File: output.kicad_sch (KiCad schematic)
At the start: 5 parts

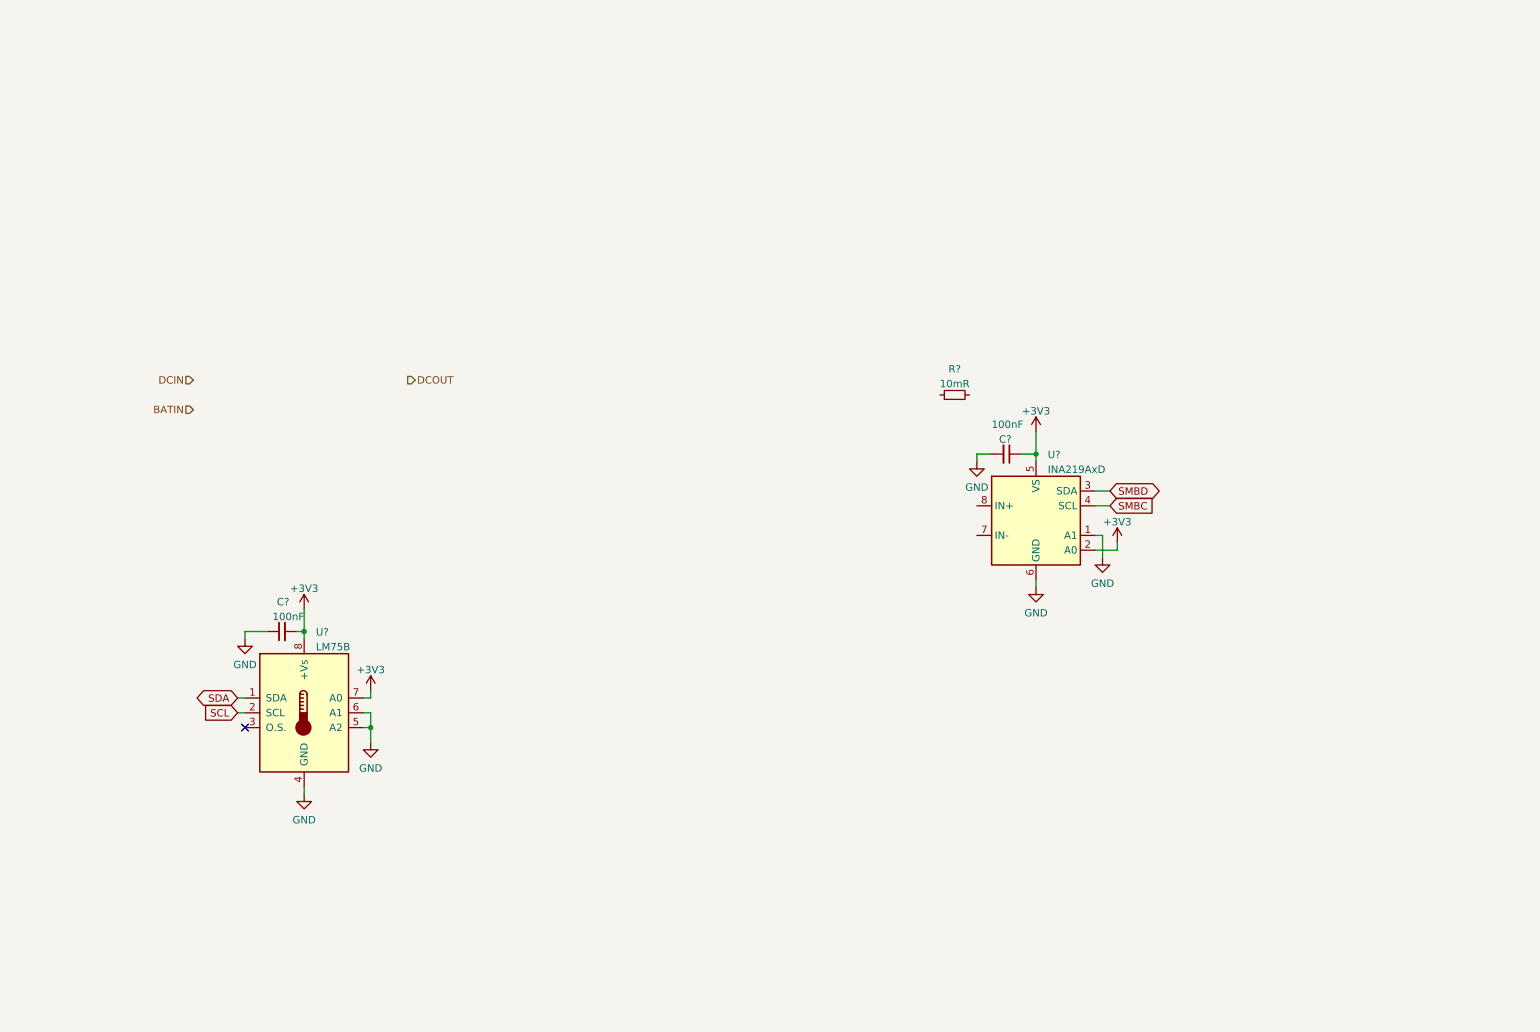
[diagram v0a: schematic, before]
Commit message: Add partial DC output circuitry
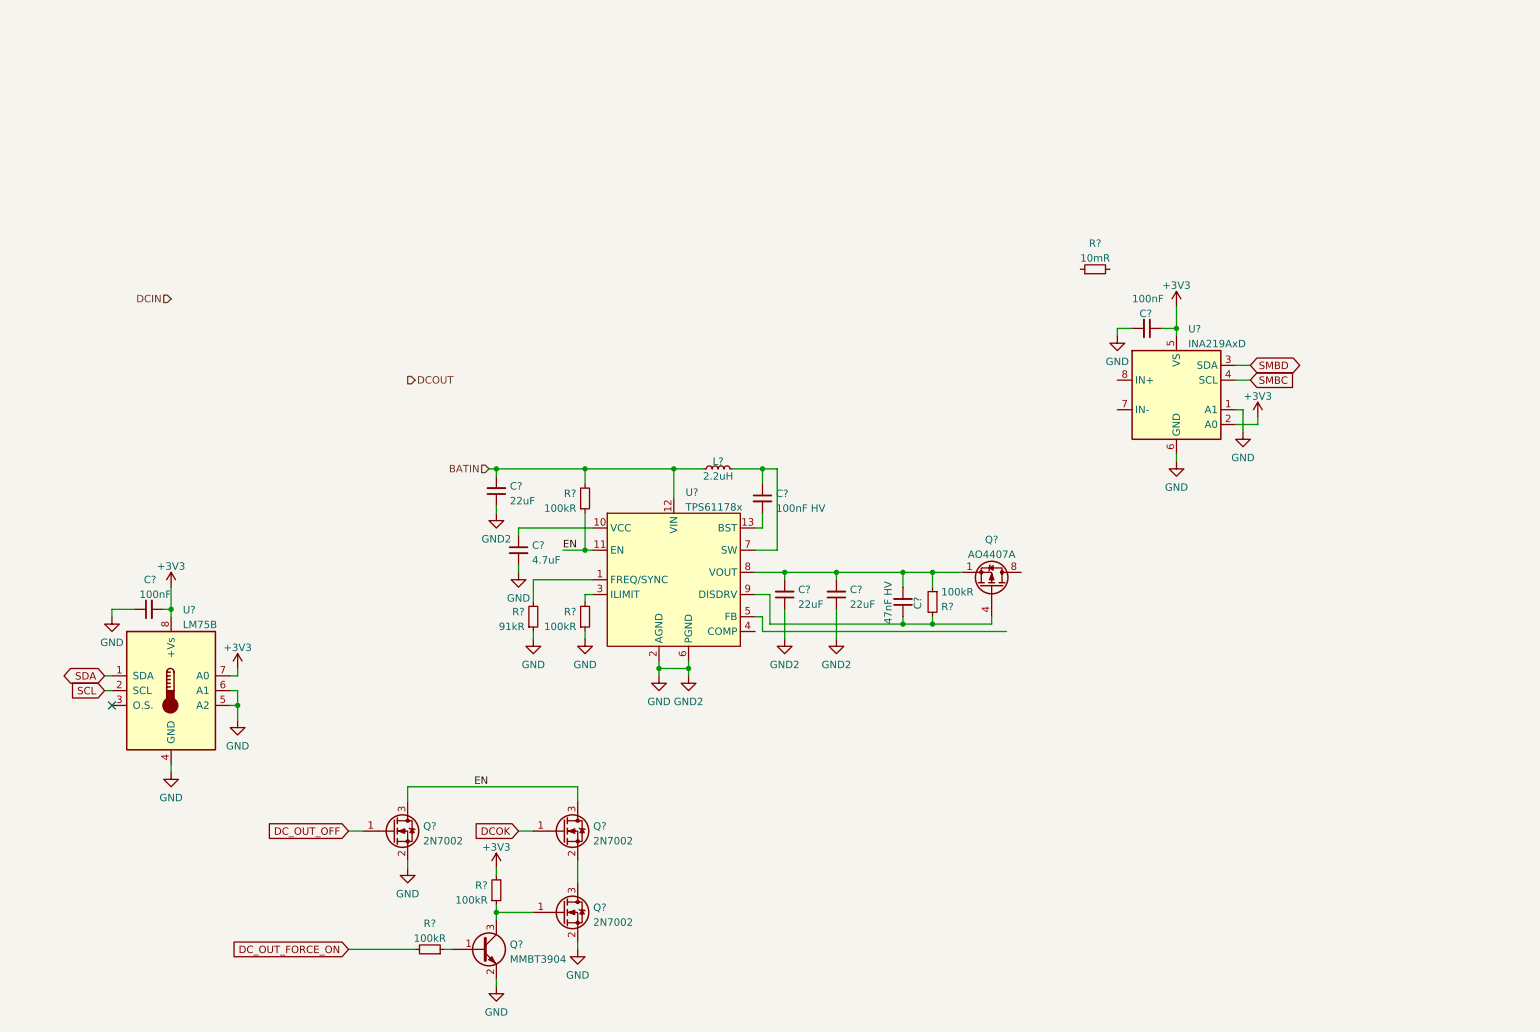
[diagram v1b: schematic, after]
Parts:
- added C?: 47nF HV, Capacitor_SMD:C_0603_1608Metric, symbol Device:C_Small
- added C? (x3): 22uF, Capacitor_SMD:C_0805_2012Metric, symbol Device:C_Small
- added C?: 100nF HV, Capacitor_SMD:C_0603_1608Metric, symbol Device:C_Small
- added C?: 4.7uF, Capacitor_SMD:C_0402_1005Metric, symbol Device:C_Small
- added L?: 2.2uH, Inductor_SMD:L_Bourns_SRP7028A_7.3x6.6mm, symbol Device:L_Small
- added Q? (x3): 2N7002, Package_TO_SOT_SMD:SOT-23, symbol Transistor_FET:2N7002
- added Q?: AO4407A, Package_SO:SOIC-8_3.9x4.9mm_P1.27mm, symbol Transistor_FET:FDS9435A
- added Q?: MMBT3904, Package_TO_SOT_SMD:SOT-23, symbol Transistor_BJT:MMBT3904
- added R?: 91kR, Resistor_SMD:R_0603_1608Metric, symbol Device:R_Small
- added R? (x5): 100kR, Resistor_SMD:R_0402_1005Metric, symbol Device:R_Small
- added U?: TPS61178x, Package_Texas:VSON-HR-13, symbol Power_Management_TI:TPS61178x
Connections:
- net +3V3: now also R?.2
- net BATIN: now also C?.2, L?.1, R?.2, U?.12 (VIN)
- net GND: now also C?.1, C?.1, C?.1, C?.2, Q?.2 (E), Q?.2 (S), Q?.2 (S), R?.1, R?.1, U?.2 (AGND), U?.6 (PGND)
- new net: Q?.1 (G), Q?.3 (C), R?.1
- new net: Q?.2 (S), Q?.3 (D)
- new net: C?.1, Q?.4 (G), R?.2, U?.9 (DISDRV)
- new net: C?.2, C?.2, C?.2, Q?.1 (S), Q?.2 (S), Q?.3 (S), R?.1, U?.8 (VOUT)
- new net: Q?.5 (D), Q?.6 (D), Q?.7 (D), Q?.8 (D)
- new net: R?.2, U?.1 (FREQ/SYNC)
- new net: C?.1, L?.2, U?.7 (SW)
- new net: C?.2, U?.13 (BST)
- new net: C?.1, U?.10 (VCC)
- new net: R?.2, U?.3 (ILIMIT)
- new net: Q?.1 (B), R?.1
- new net DCOK: Q?.1 (G)
- new net DC_OUT_FORCE_ON: R?.2
- new net DC_OUT_OFF: Q?.1 (G)
- new net EN: Q?.3 (D), Q?.3 (D), R?.1, U?.11 (EN)
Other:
- moved on the sheet: C?, R?, U?

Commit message: Finish DC output schematic capture
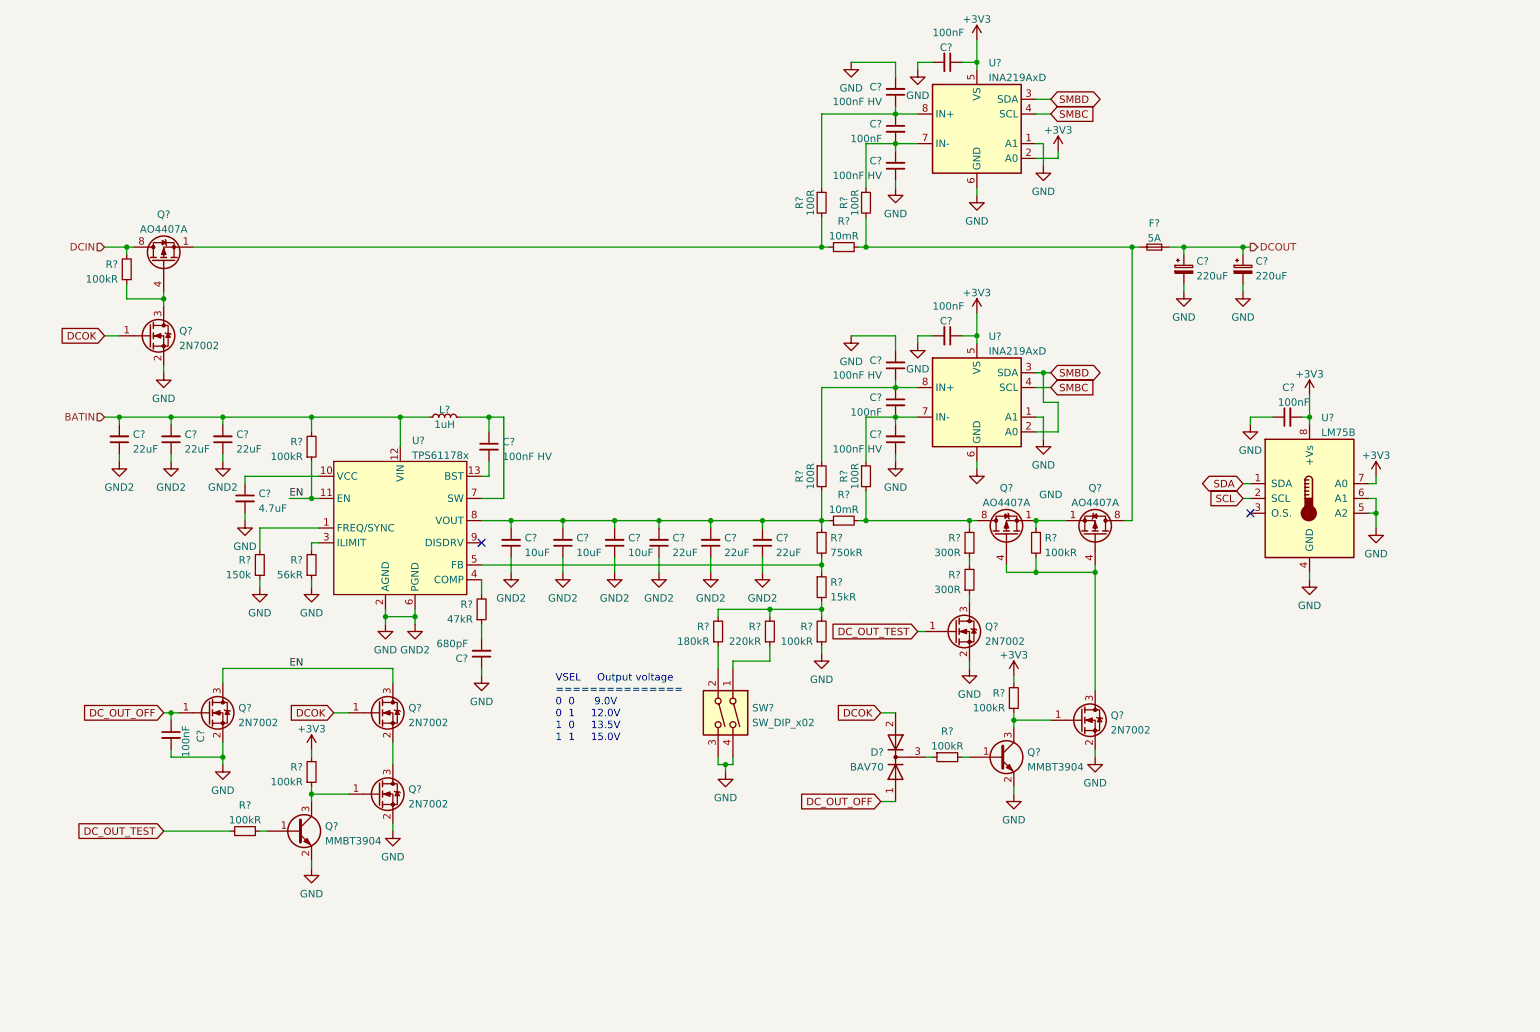
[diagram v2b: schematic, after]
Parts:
- removed C?: 47nF HV, Capacitor_SMD:C_0603_1608Metric, symbol Device:C_Small
- removed Q?: AO4407A, Package_SO:SOIC-8_3.9x4.9mm_P1.27mm, symbol Transistor_FET:FDS9435A
- removed R?: 100kR, Resistor_SMD:R_0402_1005Metric, symbol Device:R_Small
- removed R?: 10mR, Resistor_SMD:R_0805_2012Metric, symbol Device:R_Small
- removed U?: INA219AxD, Package_SO:SOIC-8_3.9x4.9mm_P1.27mm, symbol Analog_ADC:INA219AxD
- added C? (x4): 100nF, Capacitor_SMD:C_0402_1005Metric, symbol Device:C_Small
- added C? (x3): 10uF, Capacitor_SMD:C_0805_2012Metric, symbol Device:C_Small
- added C? (x4): 100nF HV, Capacitor_SMD:C_0603_1608Metric, symbol Device:C_Small
- added C? (x3): 22uF, Capacitor_SMD:C_0805_2012Metric, symbol Device:C_Small
- added C? (x2): 220uF, Capacitor_SMD:CP_Elec_6.3x7.7, symbol Device:C_Polarized_Small
- added C?: 680pF, Capacitor_SMD:C_0603_1608Metric, symbol Device:C_Small
- added D?: BAV70, Package_TO_SOT_SMD:SOT-23, symbol Diode:BAV70
- added F?: 5A, Fuse:Fuse_1206_3216Metric, symbol Device:Fuse_Small
- added Q? (x3): 2N7002, Package_TO_SOT_SMD:SOT-23, symbol Transistor_FET:2N7002
- added Q?: MMBT3904, Package_TO_SOT_SMD:SOT-23, symbol Transistor_BJT:MMBT3904
- added Q? (x3): AO4407A, Package_SO:SOIC-8_3.9x4.9mm_P1.27mm, symbol Transistor_FET:FDS9435A
- added R? (x5): 100kR, Resistor_SMD:R_0402_1005Metric, symbol Device:R_Small
- added R?: 180kR, Resistor_SMD:R_0603_1608Metric, symbol Device:R_Small
- added R? (x4): 100R, Resistor_SMD:R_0402_1005Metric, symbol Device:R_Small
- added R?: 220kR, Resistor_SMD:R_0402_1005Metric, symbol Device:R_Small
- added R? (x2): 300R, Resistor_SMD:R_1206_3216Metric, symbol Device:R_Small
- added R? (x2): 10mR, Resistor_SMD:R_0805_2012Metric, symbol Device:R_Small
- added R?: 750kR, Resistor_SMD:R_0603_1608Metric, symbol Device:R_Small
- added R?: 47kR, Resistor_SMD:R_0603_1608Metric, symbol Device:R_Small
- added R?: 15kR, Resistor_SMD:R_0402_1005Metric, symbol Device:R_Small
- added SW?: SW_DIP_x02, Connector_PinHeader_2.54mm:PinHeader_2x02_P2.54mm_Vertical, symbol Switch:SW_DIP_x02
- added U? (x2): INA219AxD, Package_SO:SOIC-8_3.9x4.9mm_P1.27mm, symbol Analog_ADC:INA219AxD
- L?: value 2.2uH -> 1uH; LCSC C76855 -> C439005
- R?: value 91kR -> 150k; footprint Resistor_SMD:R_0603_1608Metric -> Resistor_SMD:R_0402_1005Metric; LCSC C23265 -> C25755
- R?: value 100kR -> 56kR; LCSC C25741 -> C25796
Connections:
- net +3V3: now also C?.1, R?.2, U?.2 (A0), U?.5 (VS), U?.5 (VS)
- net BATIN: now also C?.2, C?.2
- net DCIN: now also Q?.5 (D), Q?.6 (D), Q?.7 (D), Q?.8 (D), R?.2
- net DCOK: now also D?.2 (A), Q?.1 (G)
- net DCOUT: now also C?.1, C?.1, F?.1
- net DC_OUT_OFF: now also C?.1, D?.1 (A)
- net GND: now also C?.1, C?.1, C?.1, C?.1, C?.1, C?.1, C?.1, C?.1, C?.1, C?.2, C?.2, C?.2, C?.2, C?.2, C?.2, Q?.2 (E), Q?.2 (S), Q?.2 (S), Q?.2 (S), R?.1, SW?.3, SW?.4, U?.1 (A1), U?.1 (A1), U?.6 (GND), U?.6 (GND)
- net SMBC: now also U?.4 (SCL), U?.4 (SCL)
- net SMBD: now also U?.2 (A0), U?.3 (SDA), U?.3 (SDA)
- net at C?.2, C?.2, U?.8 (VOUT): now also C?.2, C?.2, C?.2, C?.2, R?.1, R?.1, R?.2
- net at U?.4 (COMP): now also R?.2
- net at U?.5 (FB): now also R?.1, R?.2
- net DC_OUT_FORCE_ON renamed DC_OUT_TEST
- net DC_OUT_TEST: now also Q?.1 (G)
- new net: D?.3 (K), R?.1
- new net: Q?.1 (B), R?.2
- new net: R?.1, SW?.2
- new net: R?.2, R?.2, R?.2, R?.2
- new net: Q?.1 (S), Q?.1 (S), Q?.2 (S), Q?.2 (S), Q?.3 (S), Q?.3 (S), R?.1
- new net: Q?.3 (D), Q?.4 (G), Q?.4 (G), R?.2
- new net: Q?.3 (D), R?.1
- new net: C?.2, C?.2, R?.1, U?.7 (IN-) (x2)
- new net: F?.2, Q?.5 (D), Q?.6 (D), Q?.7 (D), Q?.8 (D), R?.2, R?.2
- new net: R?.1, SW?.1
- new net: R?.1, R?.2
- new net: Q?.5 (D), Q?.6 (D), Q?.7 (D), Q?.8 (D), R?.2, R?.2, R?.2
- new net: C?.1, C?.1, R?.1, U?.8 (IN+) (x2)
- new net: Q?.1 (G), Q?.3 (C), R?.1
- new net: Q?.3 (D), Q?.4 (G), R?.1
- new net: Q?.1 (S), Q?.2 (S), Q?.3 (S), R?.1, R?.2
- new net: C?.2, R?.1
- no-connect marks 1 -> 2
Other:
- note added: "VSEL Output voltage =============== 0 0 9.0V 0 1 12.0V 1 0 13.5V 1 1 15.0V"
- moved on the sheet: C?, L?, Q?, R?, U?

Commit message: Add barrel jack footprints
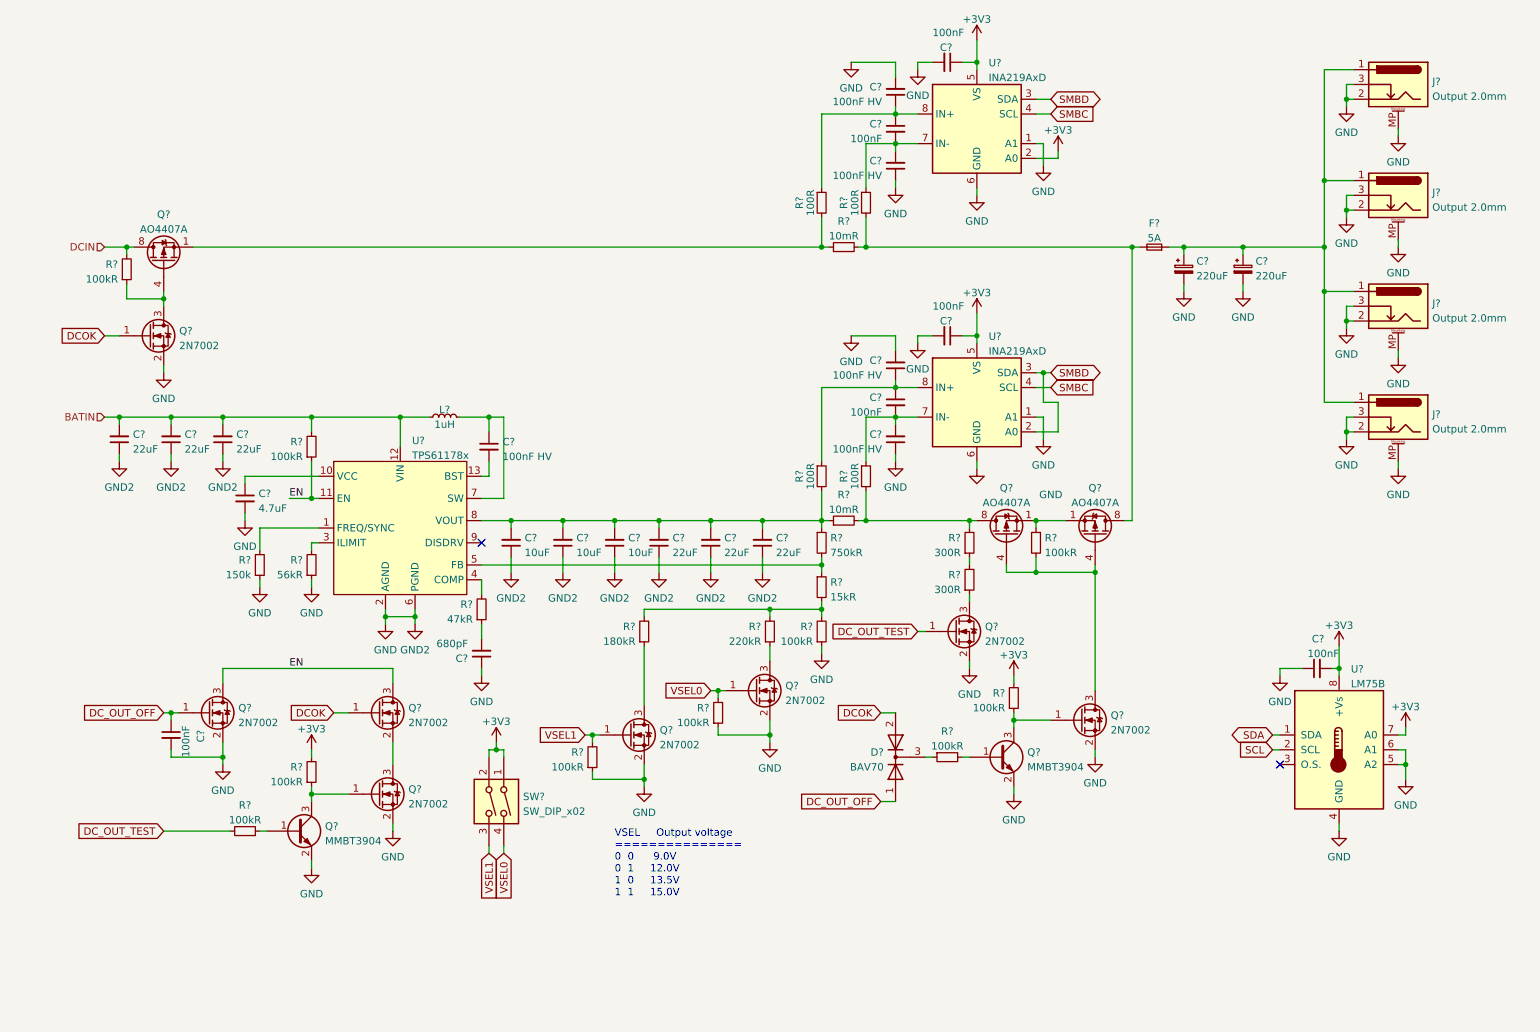
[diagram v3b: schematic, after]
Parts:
- removed U?: LM75B, symbol Sensor_Temperature:LM75B
- added J? (x4): Output 2.0mm, Connector_BarrelJack_LCSC:BarrelJack_2.0mm_DC-044B, symbol Connector:Barrel_Jack_Switch_MountingPin
- added Q? (x2): 2N7002, Package_TO_SOT_SMD:SOT-23, symbol Transistor_FET:2N7002
- added R? (x2): 100kR, Resistor_SMD:R_0402_1005Metric, symbol Device:R_Small
- added U?: LM75B, Package_SO:MSOP-8_3x3mm_P0.65mm, symbol Sensor_Temperature:LM75B
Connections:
- net +3V3: now also SW?.1, SW?.2, U?.7 (A0), U?.8 (+Vs)
- net GND: now also J?.2, J?.2, J?.2, J?.2, J?.3, J?.3, J?.3, J?.3, J?.MP (MountPin), J?.MP (MountPin), J?.MP (MountPin), J?.MP (MountPin), Q?.2 (S), Q?.2 (S), R?.1, R?.1, U?.4 (GND), U?.5 (A2), U?.6 (A1); no longer SW?.3, SW?.4
- net SCL: now also U?.2 (SCL)
- net SDA: now also U?.1 (SDA)
- net at R?.1: now also Q?.3 (D); no longer SW?.2
- net at R?.1: now also Q?.3 (D); no longer SW?.1
- net DCOUT: no longer names the net of C?.1, C?.1, F?.1
- net DCOUT: now also J?.1, J?.1, J?.1, J?.1
- new net VSEL0: Q?.1 (G), R?.2, SW?.4
- new net VSEL1: Q?.1 (G), R?.2, SW?.3
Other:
- moved on the sheet: C?, R?, SW?
